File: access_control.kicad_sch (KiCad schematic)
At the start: 0 parts

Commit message: Drew the typical operating system for MAX3232 chip
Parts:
- added U1: STM32F446RETx, Package_QFP:LQFP-64_10x10mm_P0.5mm, symbol MCU_ST_STM32F4:STM32F446RETx
- added U2: DS3231M, Package_SO:SOIC-16W_7.5x10.3mm_P1.27mm, symbol Timer_RTC:DS3231M
- added U3: MAX3232ESE, Package_SO:SOIC-16_3.9x9.9mm_P1.27mm, symbol max3232_symbol:MAX3232ESE
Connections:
- new net: U1.18 (VSS), U1.31 (VSS), U1.47 (VSS), U1.63 (VSS)
- new net: U2.10 (GND), U2.11 (GND), U2.12 (GND), U2.13 (GND), U2.5 (GND), U2.6 (GND), U2.7 (GND), U2.8 (GND), U2.9 (GND)

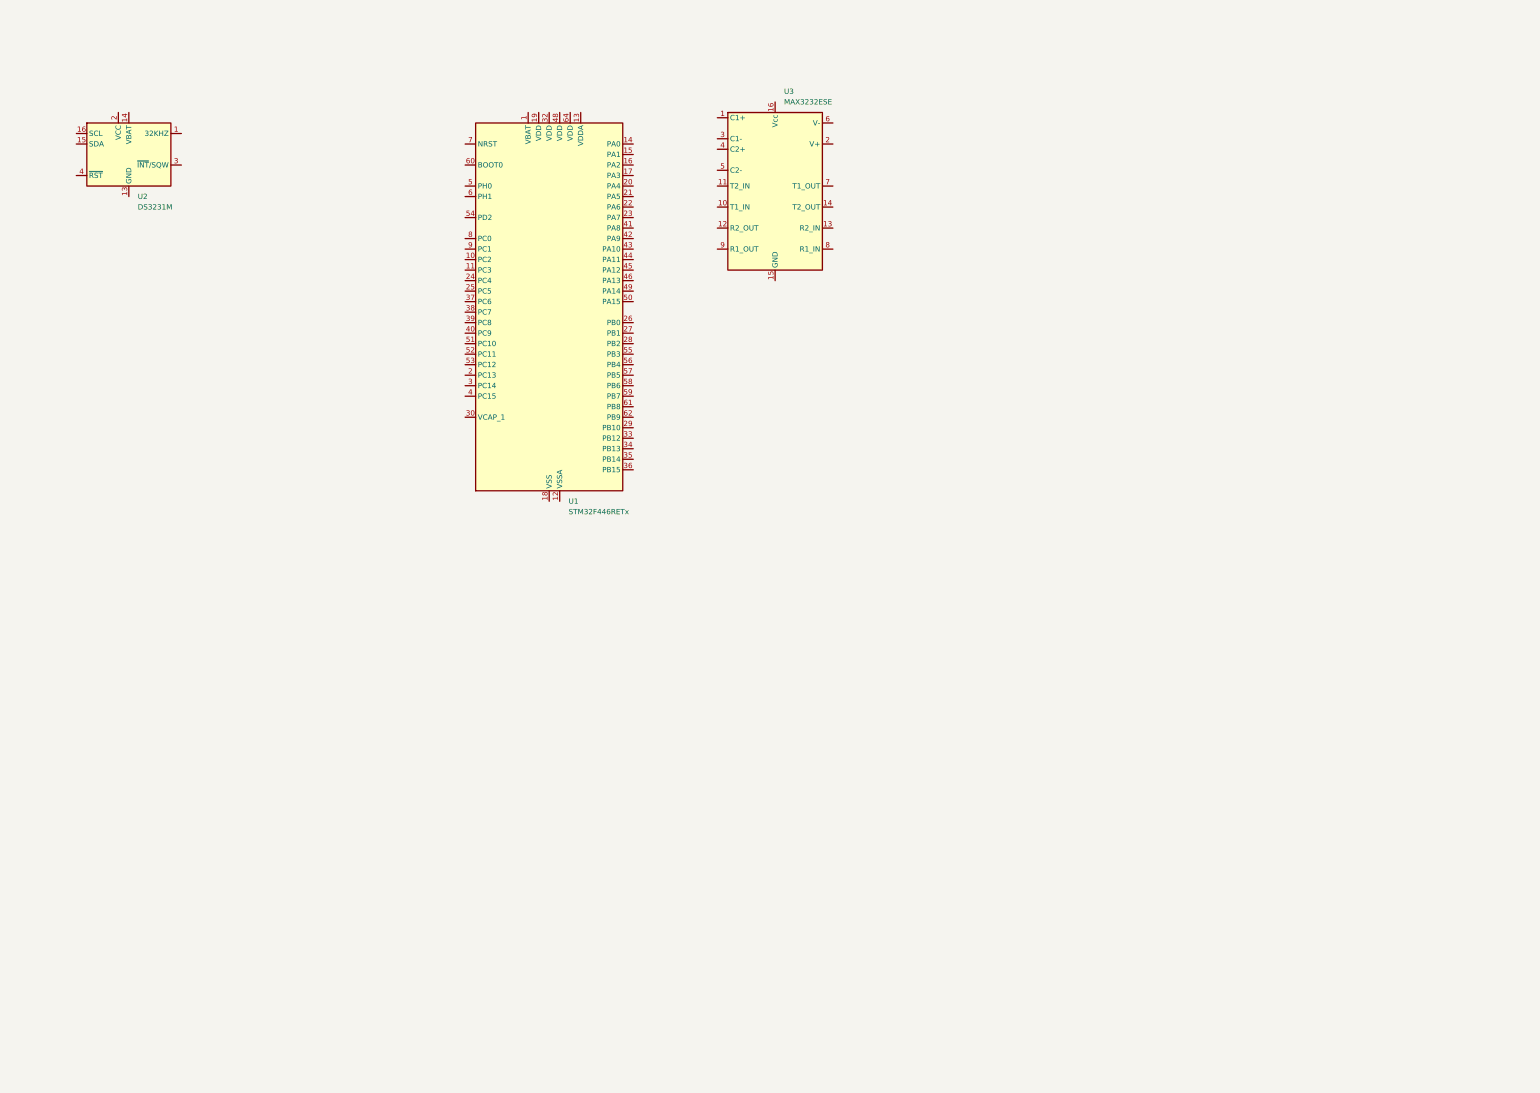
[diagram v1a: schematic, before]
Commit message: Drwe typical operating circuit for ds3231 and started with MCU's circuit
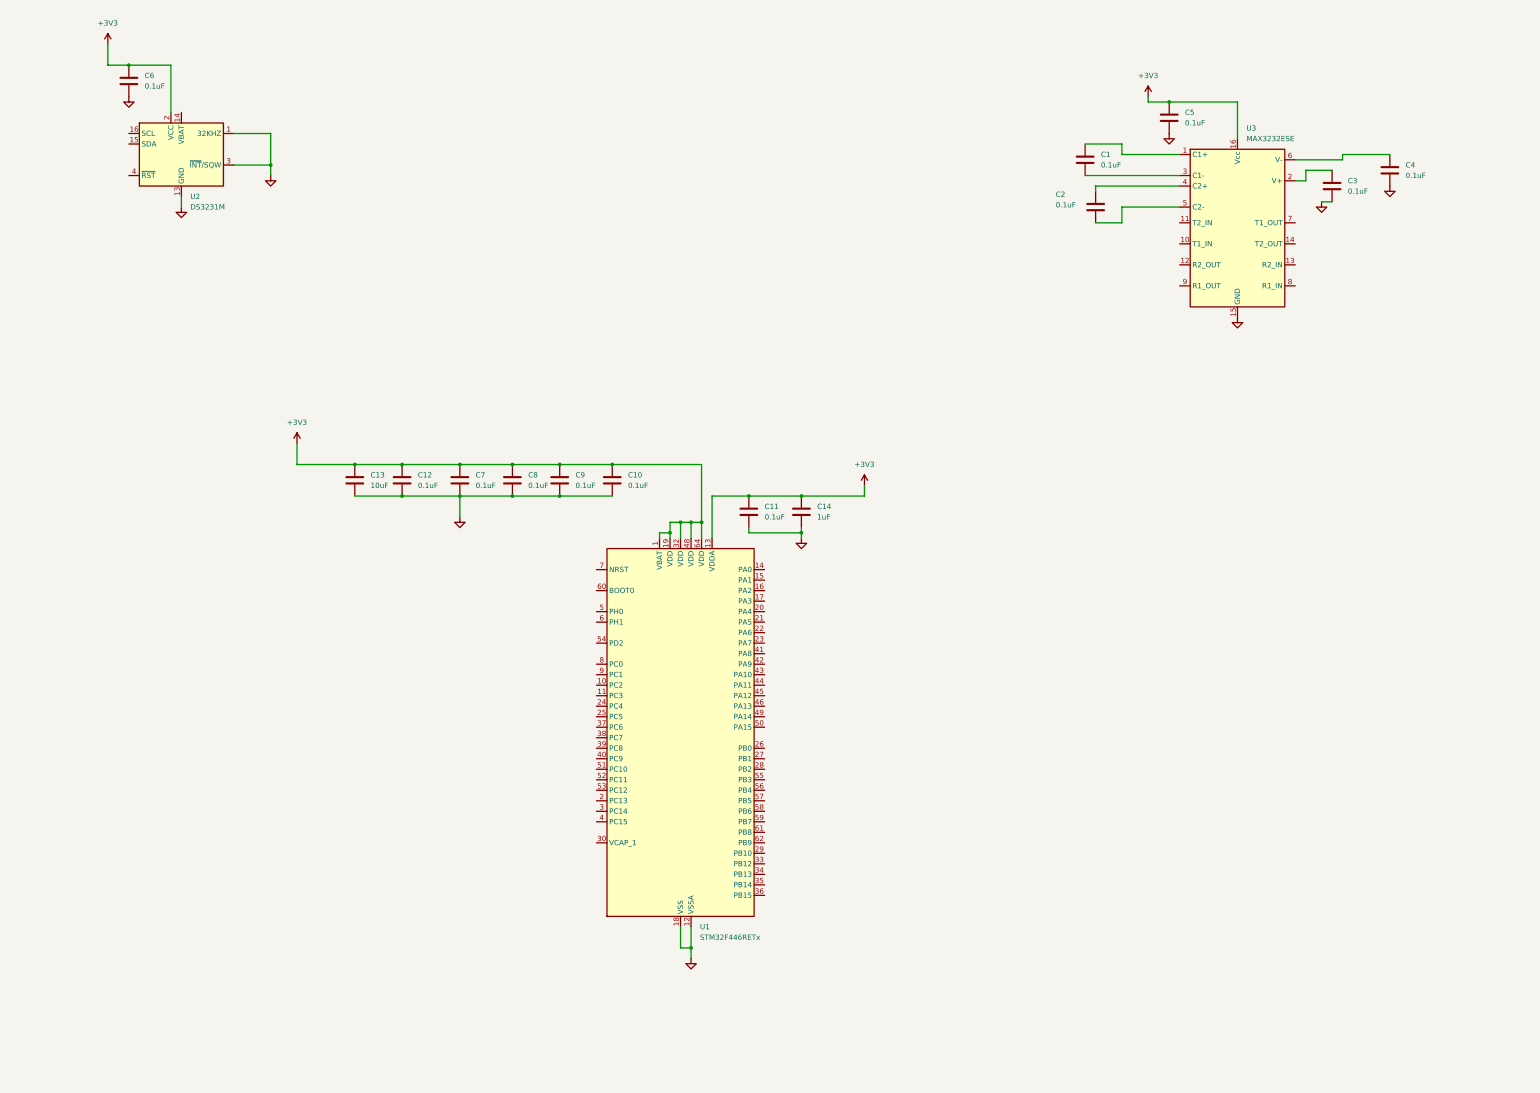
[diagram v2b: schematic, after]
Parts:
- added C1, C10, C11, C12, C2, C3, C4, C5, C6, C7, C8, C9: 0.1uF, Capacitor_SMD:C_0805_2012Metric, symbol Device:C
- added C13: 10uF, Capacitor_SMD:C_0805_2012Metric, symbol Device:C
- added C14: 1uF, Capacitor_SMD:C_0805_2012Metric, symbol Device:C
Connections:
- net at U3.1 (C1+): now also C1.1
- net GND: now reaches U3.15 (GND)
- net GND: now also U1.12 (VSSA), U1.18 (VSS), U1.31 (VSS), U1.47 (VSS), U1.63 (VSS), U2.1 (32KHZ), U2.10 (GND), U2.11 (GND), U2.12 (GND), U2.13 (GND), U2.3 (~{INT}/SQW), U2.5 (GND), U2.6 (GND), U2.7 (GND), U2.8 (GND), U2.9 (GND), C10.2, C11.2, C12.2, C13.2, C14.2, C3.2, C4.2, C5.2, C6.2, C7.2, C8.2, C9.2
- net +3V3: now reaches U3.16 (Vcc)
- net +3V3: now also U1.1 (VBAT), U1.13 (VDDA), U1.19 (VDD), U1.32 (VDD), U1.48 (VDD), U1.64 (VDD), U2.2 (VCC), C10.1, C11.1, C12.1, C13.1, C14.1, C5.1, C6.1, C7.1, C8.1, C9.1
- net at U3.2 (V+): now also C3.1
- net at U3.3 (C1-): now also C1.2
- net at U3.4 (C2+): now also C2.1
- net at U3.5 (C2-): now also C2.2
- net at U3.6 (V-): now also C4.1
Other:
- moved on the sheet: U1, U2, U3

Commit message: Added decoupling capacitors for Vdd and Vdda. Drew HSE oscillator. BOOT0 connected to ground via 10k pull-down. Boot connected to ground via capacitor and swith for manual reset option.
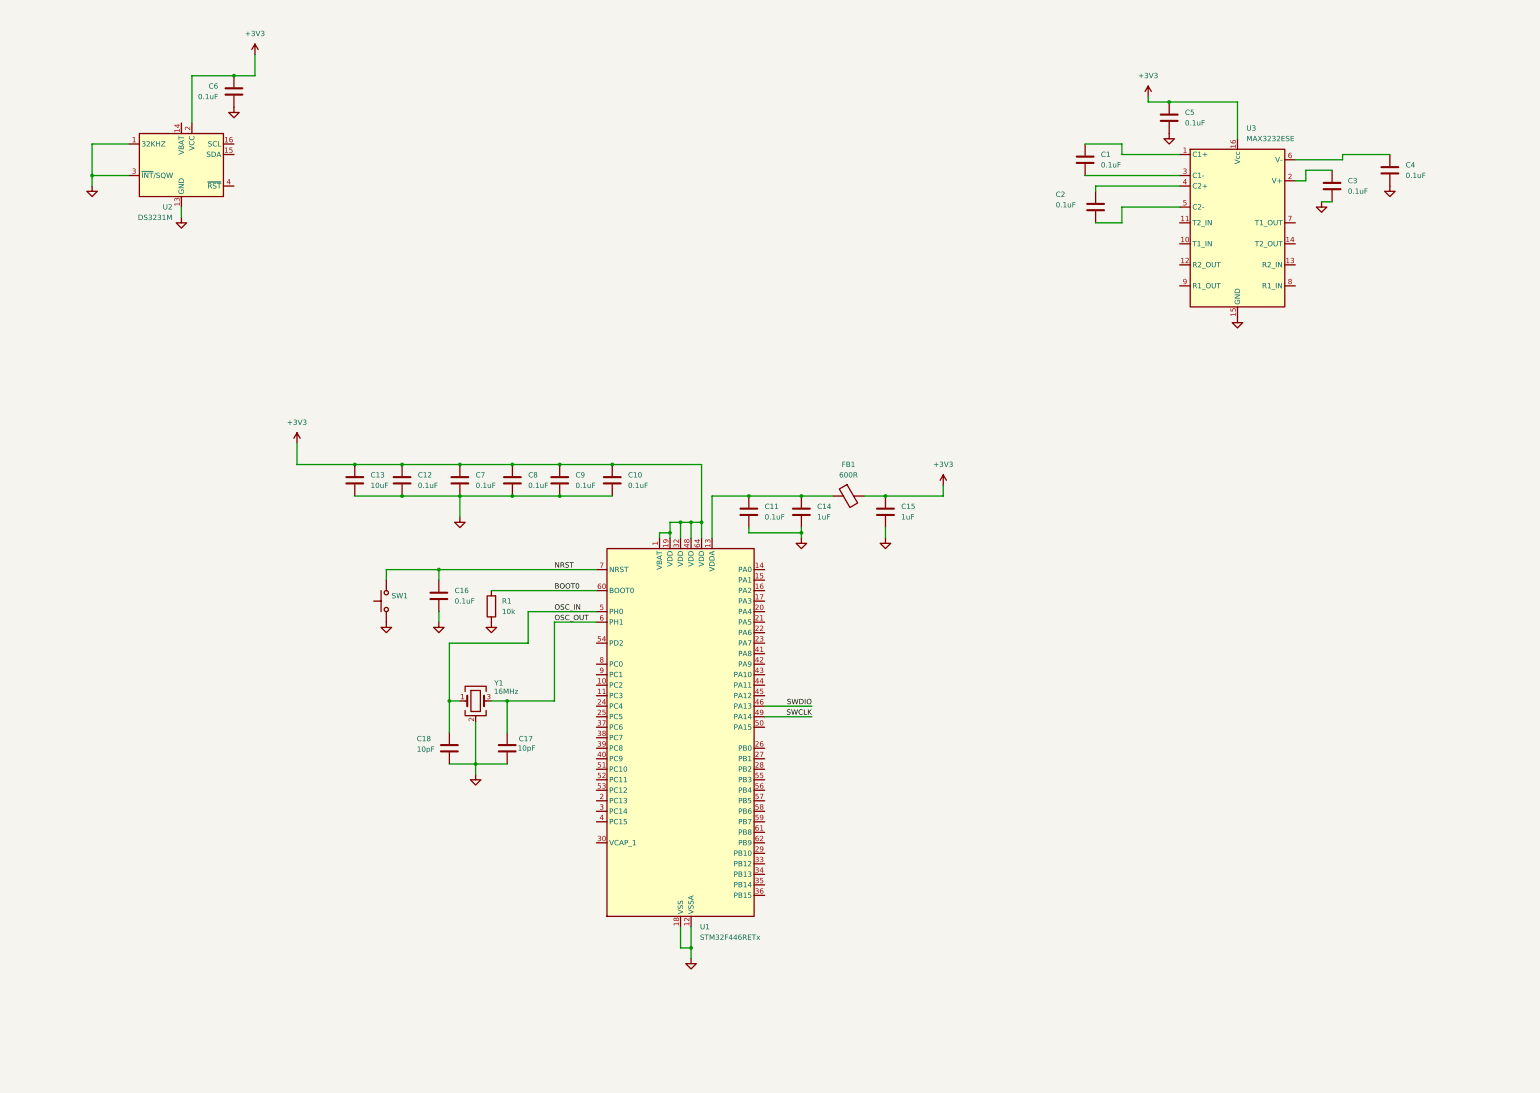
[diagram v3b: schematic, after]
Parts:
- added C15: 1uF, Capacitor_SMD:C_0805_2012Metric, symbol Device:C
- added C16: 0.1uF, Capacitor_SMD:C_0805_2012Metric, symbol Device:C
- added C17, C18: 10pF, Capacitor_SMD:C_0805_2012Metric, symbol Device:C
- added FB1: 600R, Inductor_SMD:L_0805_2012Metric_Pad1.05x1.20mm_HandSolder, symbol Device:FerriteBead
- added R1: 10k, Resistor_SMD:R_0805_2012Metric, symbol Device:R
- added SW1: Reset button, Button_Switch_SMD:SW_SPST_PTS645Sx43SMTR92, symbol Switch:SW_Push
- added Y1: 16MHz, Crystal:Crystal_SMD_3225-4Pin_3.2x2.5mm_HandSoldering, symbol Device:Crystal_GND24
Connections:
- net +3V3: now also C15.1, FB1.2; no longer C11.1, C14.1, U1.13 (VDDA)
- net GND: now also C15.2, C16.2, C17.2, C18.2, R1.1, SW1.1, Y1.2 (G), Y1.4 (G)
- net SWDIO: now reaches U1.46 (PA13)
- net SWCLK: now reaches U1.49 (PA14)
- net OSC_IN: now reaches U1.5 (PH0)
- net OSC_IN: now also C18.1, Y1.1
- net OSC_OUT: now reaches U1.6 (PH1)
- net OSC_OUT: now also C17.1, Y1.3
- net BOOT0: now reaches U1.60 (BOOT0)
- net BOOT0: now also R1.2
- net NRST: now reaches U1.7 (NRST)
- net NRST: now also C16.1, SW1.2
- new net: C11.1, C14.1, FB1.1, U1.13 (VDDA)
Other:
- moved on the sheet: C6, U2

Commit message: Added SWD connectors. Added 4.7u capacitor to VCAP_1. Changed all SMD footprints to HandSolder
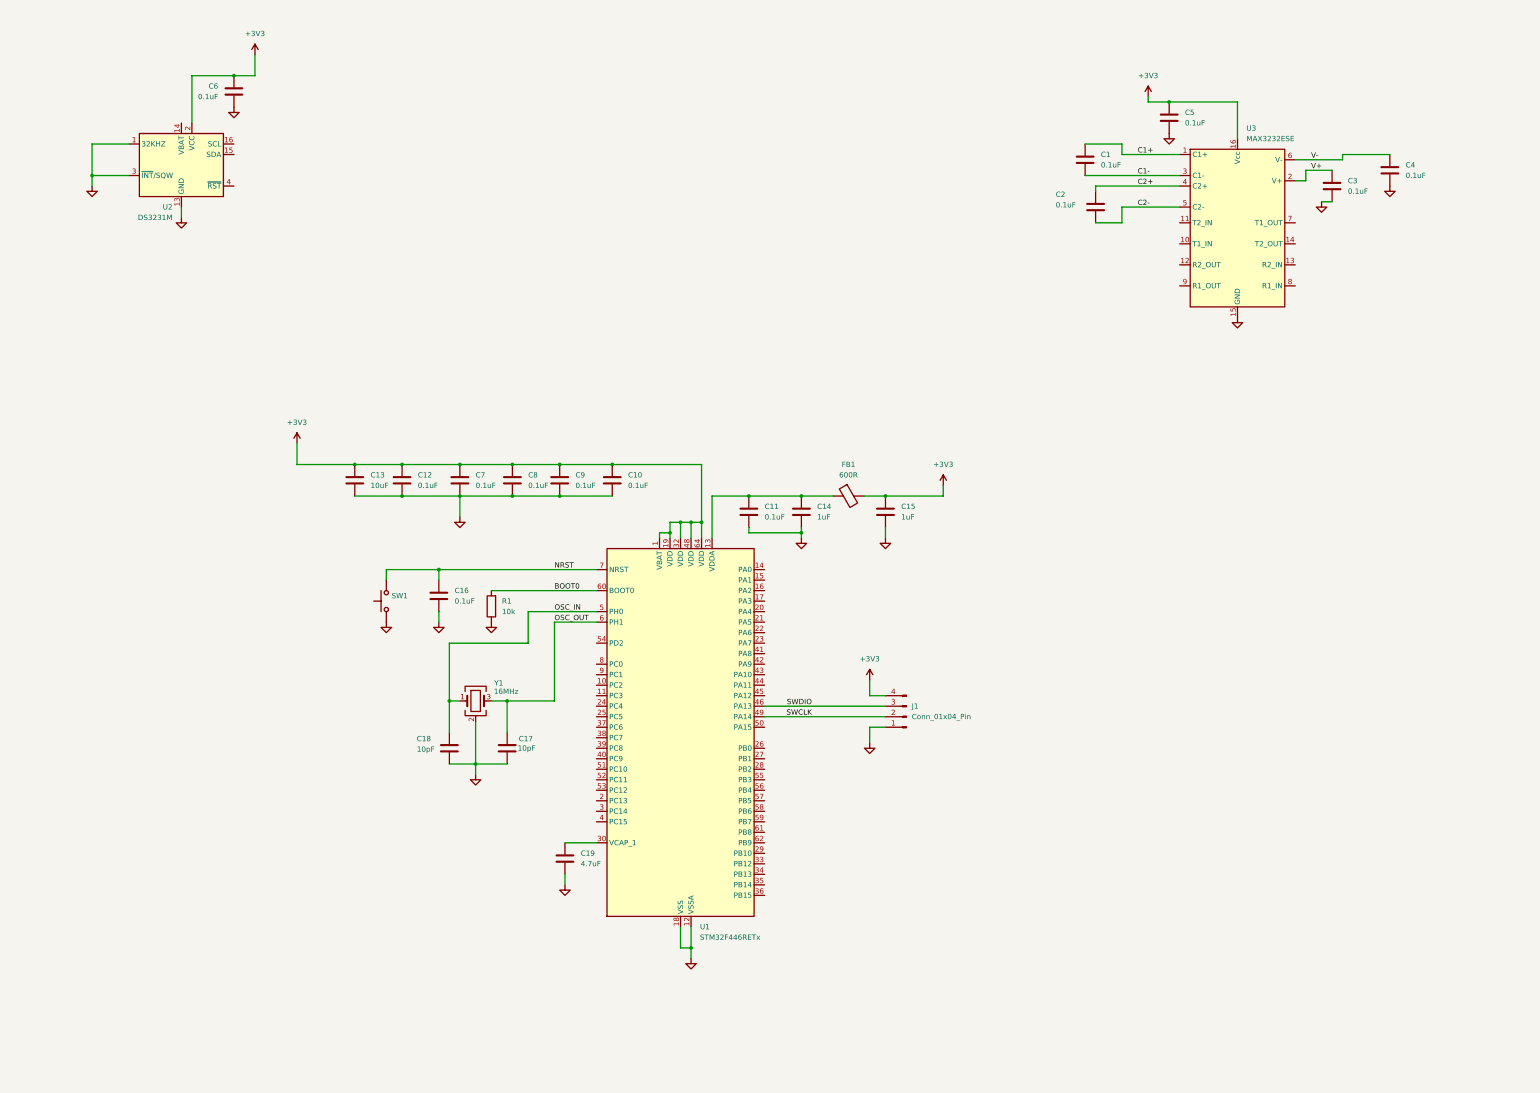
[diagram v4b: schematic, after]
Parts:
- added C19: 4.7uF, Capacitor_SMD:C_0805_2012Metric_Pad1.18x1.45mm_HandSolder, symbol Device:C
- added J1: Conn_01x04_Pin, Connector_PinHeader_2.54mm:PinHeader_1x04_P2.54mm_Vertical, symbol Connector:Conn_01x04_Pin
- C1, C10, C11, C12, C13, C14, C15, C16, C17, C18, C2, C3, C4, C5, C6, C7, C8, C9: footprint Capacitor_SMD:C_0805_2012Metric -> Capacitor_SMD:C_0805_2012Metric_Pad1.18x1.45mm_HandSolder
- R1: footprint Resistor_SMD:R_0805_2012Metric -> Resistor_SMD:R_0805_2012Metric_Pad1.20x1.40mm_HandSolder
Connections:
- net +3V3: now also J1.4 (Pin_4)
- net GND: now also C19.2, J1.1 (Pin_1)
- net SWCLK: now also J1.2 (Pin_2)
- net SWDIO: now also J1.3 (Pin_3)
- net V+: now reaches C3.1, U3.2 (V+)
- net C1+: now reaches C1.1, U3.1 (C1+)
- net C1-: now reaches C1.2, U3.3 (C1-)
- net C2+: now reaches C2.1, U3.4 (C2+)
- net C2-: now reaches C2.2, U3.5 (C2-)
- net V-: now reaches C4.1, U3.6 (V-)
- net at U1.30 (VCAP_1): now also C19.1

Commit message: Connected DS3231 and MAX3232 to the MCU
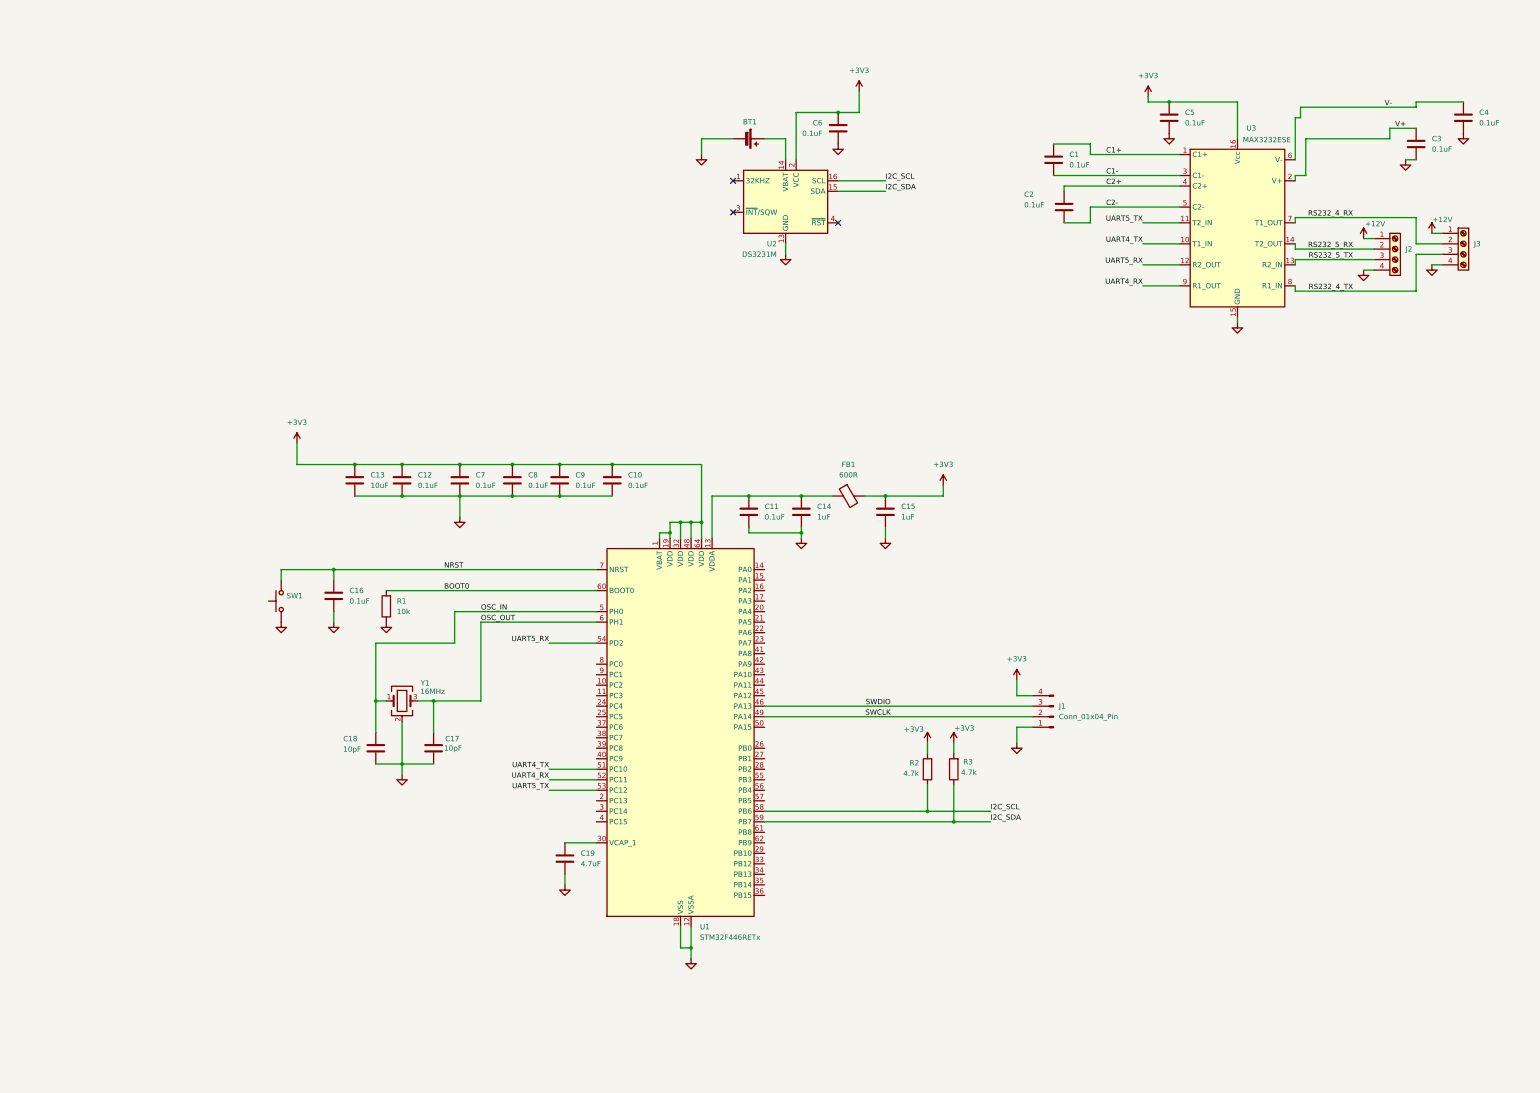
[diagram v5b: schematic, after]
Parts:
- added BT1: Battery_Cell, Battery:BatteryHolder_Keystone_1060_1x2032, symbol Device:Battery_Cell
- added J2, J3: Screw_Terminal_01x04, symbol Connector:Screw_Terminal_01x04
- added R2, R3: 4.7k, Resistor_SMD:R_0805_2012Metric_Pad1.20x1.40mm_HandSolder, symbol Device:R
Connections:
- net +3V3: now also R2.2, R3.2
- net GND: now also BT1.2 (-), J2.4 (Pin_4), J3.4 (Pin_4); no longer U2.1 (32KHZ), U2.3 (~{INT}/SQW)
- net UART4_TX: now reaches U3.10 (T1_IN)
- net UART4_TX: now also U1.51 (PC10)
- net UART5_TX: now reaches U3.11 (T2_IN)
- net UART5_TX: now also U1.53 (PC12)
- net UART5_RX: now reaches U3.12 (R2_OUT)
- net UART5_RX: now also U1.54 (PD2)
- net RS232_5_TX: now reaches U3.13 (R2_IN)
- net RS232_5_TX: now also J2.3 (Pin_3)
- net RS232_5_RX: now reaches U3.14 (T2_OUT)
- net RS232_5_RX: now also J2.2 (Pin_2)
- net RS232_4_RX: now reaches U3.7 (T1_OUT)
- net RS232_4_RX: now also J3.2 (Pin_2)
- net RS232_4_TX: now reaches U3.8 (R1_IN)
- net RS232_4_TX: now also J3.3 (Pin_3)
- net UART4_RX: now reaches U3.9 (R1_OUT)
- net UART4_RX: now also U1.52 (PC11)
- net I2C_SCL: now reaches U1.58 (PB6)
- net I2C_SCL: now also U2.16 (SCL), R2.1
- net I2C_SDA: now reaches U1.59 (PB7)
- net I2C_SDA: now also U2.15 (SDA), R3.1
- net at U2.14 (VBAT): now also BT1.1 (+)
- new net +12V: J2.1 (Pin_1), J3.1 (Pin_1)
- no-connect marks 0 -> 3
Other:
- moved on the sheet: C1, C16, C17, C18, C2, C3, C4, C6, J1, R1, SW1, U2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
